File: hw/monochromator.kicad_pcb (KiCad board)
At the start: 2 copper layers, 44 parts, among them J1 USB_B, J2 UART_01X03, J3 IDC_02X03, J4 SWD_01X04, J5 Screw_Terminal, SW1 SW_Push, U1 USBLC6-2SC6, U2 STM32F072CBTx, U3 CP2102, U4 MCP16301H

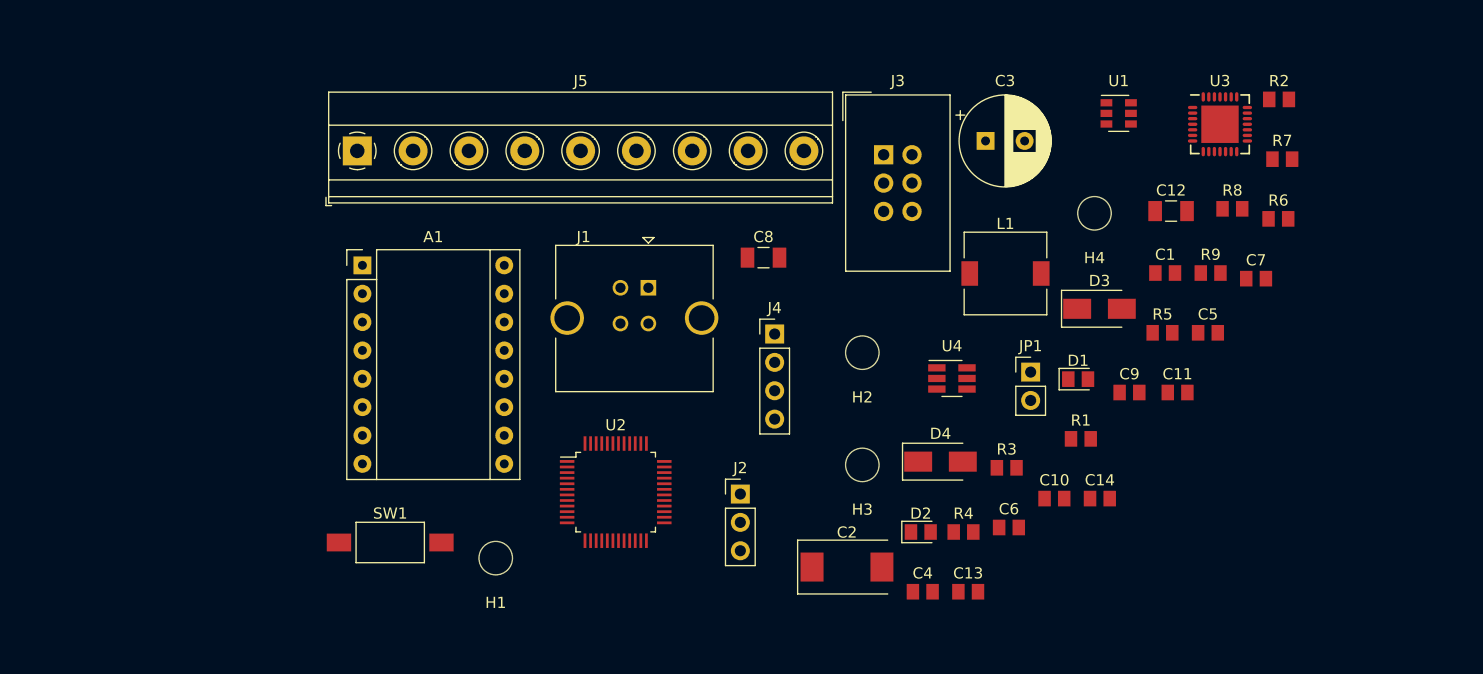
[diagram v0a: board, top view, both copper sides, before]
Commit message: add GND plate
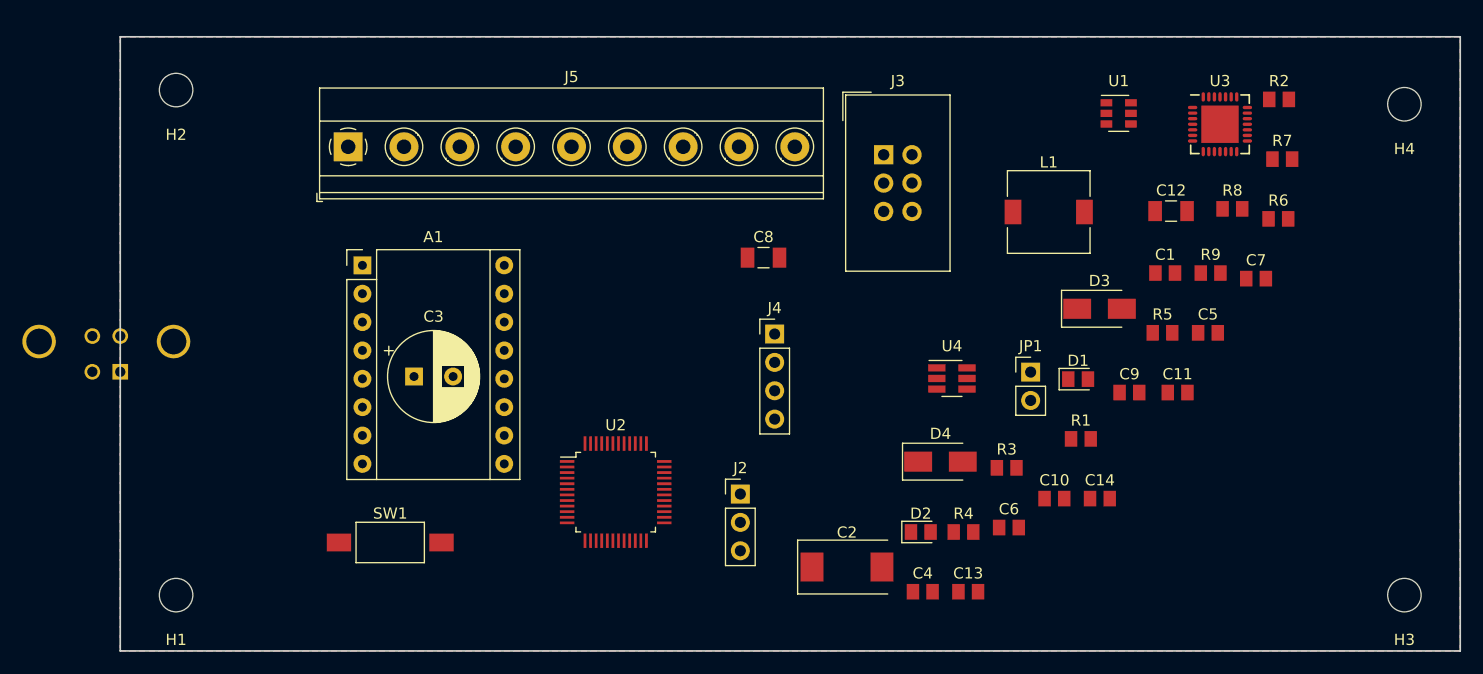
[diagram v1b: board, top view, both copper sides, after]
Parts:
- J1: moved to B.Cu
- moved H2 65.8 mm to (90.0, 64.8)
- moved C3 55.4 mm to (111.3, 90.4)
- moved H3 49.9 mm to (200.0, 110.0)
- moved J1 47.9 mm to (85.0, 90.0)
- moved H4 29.4 mm to (200.0, 66.0)
- moved H1 28.8 mm to (90.0, 110.0)
- moved L1 6.73 mm to (168.1, 75.7)
- moved J5 0.89 mm to (105.4, 69.8)
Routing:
- added copper zone on B.Cu, net GND
- added copper zone on F.Cu, net GND
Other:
- board outline added: 120 x 55 mm
- net class Default: clearance 0.2 -> 0.1
- rule trace_clearance: 0.2 -> 0.1
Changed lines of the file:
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@@
-(kicad_pcb (version 20171130) (host pcbnew 5.0.0-rc2-dev-unknown-0f0d9af~63~ubuntu16.04.1)
+(kicad_pcb (version 20171130) (host pcbnew "(5.0.0-rc2-dev-632-g76d3b6f04)")
   (general
     (thickness 1.6)
-    (drawings 0)
+    (drawings 4)
     (tracks 0)
     (zones 0)
@@
     (47 F.CrtYd user)
     (48 B.Fab user)
-    (49 F.Fab user)
+    (49 F.Fab user hide)
   )
   (setup
     (last_trace_width 0.25)
-    (trace_clearance 0.2)
+    (user_trace_width 0.5)
+    (user_trace_width 0.8)
+    (user_trace_width 1)
+    (trace_clearance 0.1)
     (zone_clearance 0.508)
     (zone_45_only no)
@@
     (pad_to_mask_clearance 0.2)
     (aux_axis_origin 0 0)
-    (visible_elements FFFFFF7F)
+    (visible_elements 7FFEF7FF)
     (pcbplotparams
       (layerselection 0x010fc_ffffffff)
@@
   (net 81 "Net-(A1-Pad13)")
   (net_class Default "Toto je výchozí třída sítě."
-    (clearance 0.2)
+    (clearance 0.1)
     (trace_width 0.25)
     (via_dia 0.8)
@@
   )
   (module Capacitor_THT:CP_Radial_D8.0mm_P3.50mm (layer F.Cu)
-    (at 162.489699 69.3275)
+    (at 111.308 90.424)
     (descr "CP, Radial series, Radial, pin pitch=3.50mm, , diameter=8mm, Electrolytic Capacitor")
     (tags "CP Radial series Radial pin pitch 3.50mm  diameter 8mm Electrolytic Capacitor")
@@
     )
   )
-  (module Connector_USB:USB_B_TE_5787834_Vertical (layer F.Cu)
-    (at 132.295001 82.4775)
+  (module Connector_USB:USB_B_TE_5787834_Vertical (layer B.Cu)
+    (at 85 90)
     (descr http://www.mouser.com/ds/2/418/NG_CD_5787834_A4-669110.pdf)
     (tags "USB_B USB B vertical female connector")
-    (fp_text reference J1 (at -5.8 -4.55) (layer F.SilkS)
-      (effects (font (size 1 1) (thickness 0.15)))
-    )
-    (fp_text value USB_B (at -1.25 10.25) (layer F.Fab)
-      (effects (font (size 1 1) (thickness 0.15)))
-    )
-    (fp_text user %R (at -1.2 6.4) (layer F.Fab)
-      (effects (font (size 1 1) (thickness 0.15)))
-    )
-    (fp_line (start -8.3 1) (end -8.3 -3.8) (layer F.SilkS) (width 0.12))
-    (fp_line (start -8.3 9.3) (end -8.3 4.5) (layer F.SilkS) (width 0.12))
-    (fp_line (start 5.8 9.3) (end -8.3 9.3) (layer F.SilkS) (width 0.12))
-    (fp_line (start 5.8 4.5) (end 5.8 9.3) (layer F.SilkS) (width 0.12))
-    (fp_line (start 5.8 -3.8) (end 5.8 1) (layer F.SilkS) (width 0.12))
-    (fp_line (start -8.3 -3.8) (end 5.8 -3.8) (layer F.SilkS) (width 0.12))
-    (fp_line (start -0.5 -4.5) (end 0 -4) (layer F.SilkS) (width 0.12))
-    (fp_line (start 0.5 -4.5) (end -0.5 -4.5) (layer F.SilkS) (width 0.12))
-    (fp_line (start 0 -4) (end 0.5 -4.5) (layer F.SilkS) (width 0.12))
-    (fp_line (start 5 -3.75) (end 5.75 -3) (layer F.Fab) (width 0.1))
-    (fp_line (start -8.25 -3.75) (end 5 -3.75) (layer F.Fab) (width 0.1))
-    (fp_line (start 5.75 -3) (end 5.75 9.25) (layer F.Fab) (width 0.1))
-    (fp_line (start 5.75 9.25) (end -8.25 9.25) (layer F.Fab) (width 0.1))
-    (fp_line (start -8.25 9.25) (end -8.25 -3.75) (layer F.Fab) (width 0.1))
-    (fp_line (start -9 -4) (end 6.5 -4) (layer F.CrtYd) (width 0.05))
-    (fp_line (start -9 -4) (end -9 9.5) (layer F.CrtYd) (width 0.05))
-    (fp_line (start 6.5 9.5) (end 6.5 -4) (layer F.CrtYd) (width 0.05))
-    (fp_line (start 6.5 9.5) (end -9 9.5) (layer F.CrtYd) (width 0.05))
-    (pad 5 thru_hole circle (at 4.77 2.71) (size 3 3) (drill 2.3) (layers *.Cu *.Mask)
-      (net 2 GND))
-    (pad 4 thru_hole circle (at 0 3.2) (size 1.4 1.4) (drill 0.92) (layers *.Cu *.Mask)
-      (net 2 GND))
-    (pad 3 thru_hole circle (at -2.5 3.2) (size 1.4 1.4) (drill 0.92) (layers *.Cu *.Mask)
+    (fp_text reference J1 (at -5.8 4.55) (layer B.SilkS)
+      (effects (font (size 1 1) (thickness 0.15)) (justify mirror))
+    )
+    (fp_text value USB_B (at -1.25 -10.25) (layer B.Fab)
+      (effects (font (size 1 1) (thickness 0.15)) (justify mirror))
+    )
+    (fp_text user %R (at -1.2 -6.4) (layer B.Fab)
+      (effects (font (size 1 1) (thickness 0.15)) (justify mirror))
+    )
+    (fp_line (start -8.3 -1) (end -8.3 3.8) (layer B.SilkS) (width 0.12))
+    (fp_line (start -8.3 -9.3) (end -8.3 -4.5) (layer B.SilkS) (width 0.12))
+    (fp_line (start 5.8 -9.3) (end -8.3 -9.3) (layer B.SilkS) (width 0.12))
+    (fp_line (start 5.8 -4.5) (end 5.8 -9.3) (layer B.SilkS) (width 0.12))
+    (fp_line (start 5.8 3.8) (end 5.8 -1) (layer B.SilkS) (width 0.12))
+    (fp_line (start -8.3 3.8) (end 5.8 3.8) (layer B.SilkS) (width 0.12))
+    (fp_line (start -0.5 4.5) (end 0 4) (layer B.SilkS) (width 0.12))
+    (fp_line (start 0.5 4.5) (end -0.5 4.5) (layer B.SilkS) (width 0.12))
+    (fp_line (start 0 4) (end 0.5 4.5) (layer B.SilkS) (width 0.12))
+    (fp_line (start 5 3.75) (end 5.75 3) (layer B.Fab) (width 0.1))
+    (fp_line (start -8.25 3.75) (end 5 3.75) (layer B.Fab) (width 0.1))
+    (fp_line (start 5.75 3) (end 5.75 -9.25) (layer B.Fab) (width 0.1))
+    (fp_line (start 5.75 -9.25) (end -8.25 -9.25) (layer B.Fab) (width 0.1))
+    (fp_line (start -8.25 -9.25) (end -8.25 3.75) (layer B.Fab) (width 0.1))
+    (fp_line (start -9 4) (end 6.5 4) (layer B.CrtYd) (width 0.05))
+    (fp_line (start -9 4) (end -9 -9.5) (layer B.CrtYd) (width 0.05))
+    (fp_line (start 6.5 -9.5) (end 6.5 4) (layer B.CrtYd) (width 0.05))
+    (fp_line (start 6.5 -9.5) (end -9 -9.5) (layer B.CrtYd) (width 0.05))
+    (pad 5 thru_hole circle (at 4.77 -2.71) (size 3 3) (drill 2.3) (layers *.Cu *.Mask)
+      (net 2 GND))
+    (pad 4 thru_hole circle (at 0 -3.2) (size 1.4 1.4) (drill 0.92) (layers *.Cu *.Mask)
+      (net 2 GND))
+    (pad 3 thru_hole circle (at -2.5 -3.2) (size 1.4 1.4) (drill 0.92) (layers *.Cu *.Mask)
       (net 20 "Net-(J1-Pad3)"))
     (pad 1 thru_hole rect (at 0 0) (size 1.4 1.4) (drill 0.92) (layers *.Cu *.Mask)
       (net 24 "Net-(C1-Pad1)"))
-    (pad 5 thru_hole circle (at -7.27 2.71) (size 3 3) (drill 2.3) (layers *.Cu *.Mask)
+    (pad 5 thru_hole circle (at -7.27 -2.71) (size 3 3) (drill 2.3) (layers *.Cu *.Mask)
       (net 2 GND))
     (pad 2 thru_hole circle (at -2.5 0) (size 1.4 1.4) (drill 0.92) (layers *.Cu *.Mask)
@@
   )
   (module Inductor_SMD:L_7.3x7.3_H4.5 (layer F.Cu)
-    (at 164.273571 81.1975)
+    (at 168.148 75.692)
     (descr "Choke, SMD, 7.3x7.3mm 4.5mm height")
     (tags "Choke SMD")
@@
   )
   (module KLIB_Mechanical:Bolt_M3 (layer F.Cu)
-    (at 118.625001 106.6875)
+    (at 90 110)
     (descr ~)
     (tags "bolt M3")
@@
   )
   (module KLIB_Mechanical:Bolt_M3 (layer F.Cu)
-    (at 151.455001 88.2875)
+    (at 90 64.77)
     (descr ~)
     (tags "bolt M3")
@@
   )
   (module KLIB_Mechanical:Bolt_M3 (layer F.Cu)
-    (at 151.455001 98.3375)
+    (at 200 110)
     (descr ~)
     (tags "bolt M3")
@@
   )
   (module KLIB_Mechanical:Bolt_M3 (layer F.Cu)
-    (at 172.245001 75.8075)
+    (at 200 66.04)
     (descr ~)
     (tags "bolt M3")
@@
   )
   (module TerminalBlock_Phoenix:TerminalBlock_Phoenix_MKDS-1,5-9_1x09_P5.00mm_Horizontal (layer F.Cu)
-    (at 106.225001 70.2175)
+    (at 105.41 69.85)
     (descr "Terminal Block Phoenix MKDS-1,5-9, 9 pins, pitch 05mm, size 45.0x9.8mm^2, drill diamater 1.3mm, pad diameter 2.6mm, see http://www.farnell.com/datasheets/100425.pdf, script-generated using https://github.com/pointhi/kicad-footprint-generator/scripts/TerminalBlock_Phoenix")
     (tags "THT Terminal Block Phoenix MKDS-1.5-9 pitch 05mm size 45.0x9.8mm^2 drill 1.3mm pad 2.6mm")
@@
     )
   )
+  (gr_line (start 85 115) (end 85 60) (layer Edge.Cuts) (width 0.15))
+  (gr_line (start 205 115) (end 85 115) (layer Edge.Cuts) (width 0.15))
+  (gr_line (start 205 60) (end 205 115) (layer Edge.Cuts) (width 0.15))
+  (gr_line (start 85 60) (end 205 60) (layer Edge.Cuts) (width 0.15))
+  (zone (net 2) (net_name GND) (layer F.Cu) (hatch edge 0.508)
+    (connect_pads (clearance 0.508))
+    (min_thickness 0.254)
+    (fill yes (arc_segments 16) (thermal_gap 0.508) (thermal_bridge_width 0.508))
+    (polygon
+      (pts
+        (xy 85 60) (xy 85 115) (xy 205 115) (xy 205 60)
+      )
+    )
+  )
+  (zone (net 2) (net_name GND) (layer B.Cu) (hatch edge 0.508)
+    (connect_pads (clearance 0.508))
+    (min_thickness 0.254)
+    (fill yes (arc_segments 16) (thermal_gap 0.508) (thermal_bridge_width 0.508))
+    (polygon
+      (pts
+        (xy 85 60) (xy 205 60) (xy 205 115) (xy 85 115)
+      )
+    )
+  )

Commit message: PCB layout v1.0
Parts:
- added J6: Screw_Terminal, TerminalBlock_Phoenix:TerminalBlock_Phoenix_MKDS-1,5-7_1x07_P5.00mm_Horizontal, F.Cu at (132.2, 66.0)
- C1, C14, R5, U1, U3: moved to B.Cu
- J5: value Screw_Terminal -> Power_Terminal; footprint TerminalBlock_Phoenix:TerminalBlock_Phoenix_MKDS-1,5-9_1x09_P5.00mm_Horizontal -> TerminalBlock_Phoenix:TerminalBlock_Phoenix_MKDS-1,5-2_1x02_P5.00mm_Horizontal
- moved J1 100.2 mm to (185.0, 84.2)
- moved C5 72.7 mm to (109.8, 90.7), turned to 180 degrees
- moved D3 68.1 mm to (105.1, 92.7), turned to 270 degrees
- moved R8 66.6 mm to (118.1, 77.7), turned to 180 degrees
- moved R9 64.9 mm to (118.1, 74.9)
- moved J2 64.0 mm to (199.0, 75.0)
- moved SW1 62.3 mm to (171.2, 99.8), turned to 180 degrees
- moved C12 61.8 mm to (117.6, 80.9), turned to 180 degrees
- moved L1 56.5 mm to (115.8, 96.9)
- moved C2 50.8 mm to (108.6, 78.2), turned to 90 degrees
- moved U4 49.9 mm to (109.8, 85.4), turned to 180 degrees
- moved R2 46.9 mm to (153.8, 96.8), turned to 180 degrees
- moved J4 42.5 mm to (183.8, 100.5), turned to 90 degrees
- moved D4 42.1 mm to (117.1, 90.4)
- moved A1 38.4 mm to (145.0, 77.5), turned to 270 degrees
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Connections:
- J3 pad 3: /UART_PANEL_RX -> /UART_PANEL_TX
- J3 pad 5: /UART_PANEL_TX -> /UART_PANEL_RX
- R6 pad 1: /END_STOP2 -> /END_STOP1
- R7 pad 1: /END_STOP1 -> /END_STOP2
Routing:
- net +3V3: track 0.00 -> 215.3 mm, vias 0 -> 2
- net +12V: track 0.00 -> 77.5 mm
- net /SWD_IO: track 0.00 -> 46.6 mm, vias 0 -> 2
- net /UART_USB_RX: track 0.00 -> 43.3 mm, vias 0 -> 1
- net /SWD_CLK: track 0.00 -> 42.7 mm, vias 0 -> 2
- net /UART_DEBUG_RX: track 0.00 -> 39.9 mm, vias 0 -> 1
- net /UART_USB_TX: track 0.00 -> 39.5 mm, vias 0 -> 1
- net /UART_DEBUG_TX: track 0.00 -> 37.9 mm, vias 0 -> 1
- net /~ENA: track 0.00 -> 37.4 mm, vias 0 -> 1
- net /UART_PANEL_RX: track 0.00 -> 35.5 mm, vias 0 -> 1
- net /UART_PANEL_TX: track 0.00 -> 34.4 mm, vias 0 -> 1
- net /MS0: track 0.00 -> 33.5 mm, vias 0 -> 1
- net Net-(C1-Pad1): track 0.00 -> 32.7 mm
- net /MS1: track 0.00 -> 29.7 mm, vias 0 -> 1
- net /MS2: track 0.00 -> 25.9 mm, vias 0 -> 1
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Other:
- board size 120 x 55 mm -> 120 x 45 mm

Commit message: updated power layout
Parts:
- moved C12 14.8 mm to (117.2, 95.7), turned to 270 degrees
- moved R9 14.8 mm to (119.7, 89.6), turned to 270 degrees
- moved R8 12.0 mm to (117.6, 89.6), turned to 90 degrees
- moved C8 10.7 mm to (114.6, 95.7), turned to 270 degrees
- moved L1 8.14 mm to (108.1, 94.3)
- moved D3 4.94 mm to (103.4, 88.0), turned to 180 degrees
- moved C2 2.96 mm to (109.9, 80.8), turned to 0 degrees
- moved D4 2.59 mm to (114.6, 89.6), turned to 270 degrees
- moved C5 2.06 mm to (109.8, 88.6)
- moved C9 1.36 mm to (164.3, 92.9)
- moved C4 1.24 mm to (151.9, 89.1), turned to 180 degrees
- moved C11 1.06 mm to (168.2, 89.1)
- moved C7 1.06 mm to (168.2, 85.1)
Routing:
- net +3V3: track 215.3 -> 35.2 mm, vias 2 -> 0
- net +12V: track 77.5 -> 62.0 mm
- net Net-(C5-Pad2): track 17.8 -> 12.7 mm
- net Net-(R8-Pad2): track 14.2 -> 11.8 mm
- net Net-(C5-Pad1): track 10.9 -> 8.57 mm
- net GND: track 4.81 -> 2.66 mm
- net /~RST: track 24.5 -> 26.7 mm
- net /~ENA: track 37.4 -> 36.6 mm
- net /SWD_IO: track 46.6 -> 47.2 mm
- net /MS0: track 33.5 -> 32.9 mm
- added copper zone on F.Cu, net +3V3

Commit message: ver2
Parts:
- C1, C14, R5, U1, U3: moved to F.Cu
- moved J2 32.7 mm to (169.6, 89.3)
- moved J4 30.2 mm to (153.6, 99.1)
- moved D2 23.4 mm to (169.7, 68.5)
- moved R3 23.4 mm to (169.7, 64.7)
- moved D1 22.5 mm to (172.2, 68.6)
- moved R1 22.5 mm to (172.2, 64.8)
- moved A1 15.6 mm to (129.5, 75.5), turned to 0 degrees
- moved R4 13.8 mm to (150.9, 94.2), turned to 270 degrees
- moved C3 13.1 mm to (134.1, 93.2), turned to 0 degrees
- moved JP1 12.3 mm to (146.0, 100.5), turned to 270 degrees
- moved C11 11.6 mm to (158.2, 94.9), turned to 270 degrees
- moved R2 11.1 mm to (142.7, 96.7)
- moved C9 10.2 mm to (154.2, 94.2), turned to 270 degrees
- moved J1 8.33 mm to (193.3, 85.0)
- moved U3 8.21 mm to (180.3, 91.5), turned to 0 degrees
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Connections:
- J6 pad 1: /B2 -> /A2
- J6 pad 2: /B1 -> /A1
- J6 pad 3: /A1 -> /B1
- J6 pad 4: /A2 -> /B2
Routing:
- net +3V3: track 35.2 -> 179.0 mm
- net /UART_DEBUG_RX: track 39.9 -> 9.42 mm, vias 1 -> 0
- net /UART_DEBUG_TX: track 37.9 -> 11.9 mm, vias 1 -> 0
- net Net-(U1-Pad6): track 7.89 -> 30.1 mm
- net /~ENA: track 36.6 -> 15.6 mm, vias 1 -> 0
- net /SWD_CLK: track 42.8 -> 22.3 mm, vias 2 -> 1
- net /LED1: track 4.37 -> 24.6 mm, vias 0 -> 2
- net /B2: track 11.5 -> 31.3 mm
- net /MS0: track 32.9 -> 13.8 mm, vias 1 -> 0
- net Net-(U1-Pad4): track 11.6 -> 30.1 mm, vias 2 -> 0
- net /MS1: track 29.3 -> 12.0 mm, vias 1 -> 0
- net /SWD_IO: track 47.2 -> 30.1 mm, vias 2 -> 1
- net /LED2: track 7.99 -> 24.6 mm, vias 0 -> 2
- net +12V: track 62.0 -> 78.0 mm
- net /END_STOP1: track 16.1 -> 31.1 mm, vias 0 -> 2
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
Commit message: desk v2
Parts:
- moved J1 9.00 mm to (184.3, 84.8)
- moved U3 7.34 mm to (184.8, 97.3)
- moved C1 2.47 mm to (197.1, 94.8)
- moved U1 2.40 mm to (192.4, 94.8)
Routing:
- net Net-(J1-Pad3): track 10.4 -> 19.7 mm
- net +3V3: track 179.0 -> 188.2 mm
- net Net-(J1-Pad2): track 6.42 -> 15.2 mm
- net Net-(C1-Pad1): track 35.5 -> 42.7 mm
- net /UART_USB_TX: track 31.6 -> 38.5 mm
- net Net-(R5-Pad2): track 8.22 -> 14.9 mm
- net /UART_USB_RX: track 31.3 -> 37.8 mm
- net Net-(U1-Pad6): track 30.1 -> 24.1 mm
- net Net-(U1-Pad4): track 30.1 -> 24.1 mm
- net GND: track 6.87 -> 8.96 mm
- net /~RST: track 32.5 -> 31.7 mm
